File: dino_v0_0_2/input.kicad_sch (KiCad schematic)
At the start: 11 parts, among them SW1 SW_DIP_x08

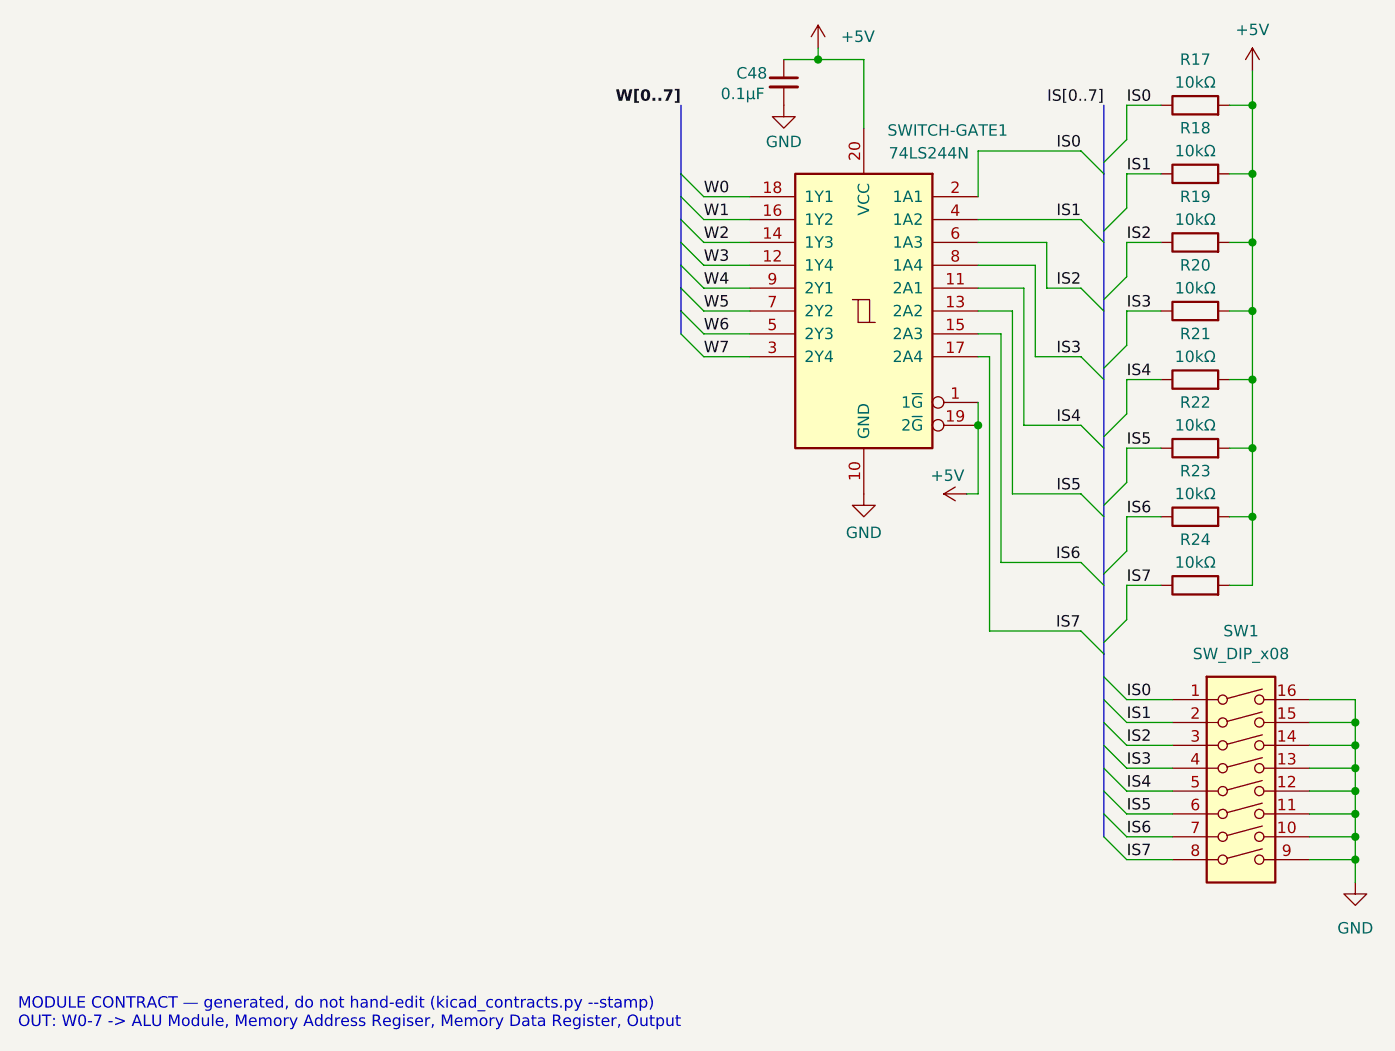
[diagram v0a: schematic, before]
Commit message: feat: card zero's '138 lands in schematic
U76 decodes M11-M13 with E1 on ~{IO_RD_Q}; O0 drives SWITCH_EN
to SWITCH-GATE1's two ~G pins, replacing step A's +5V strap.
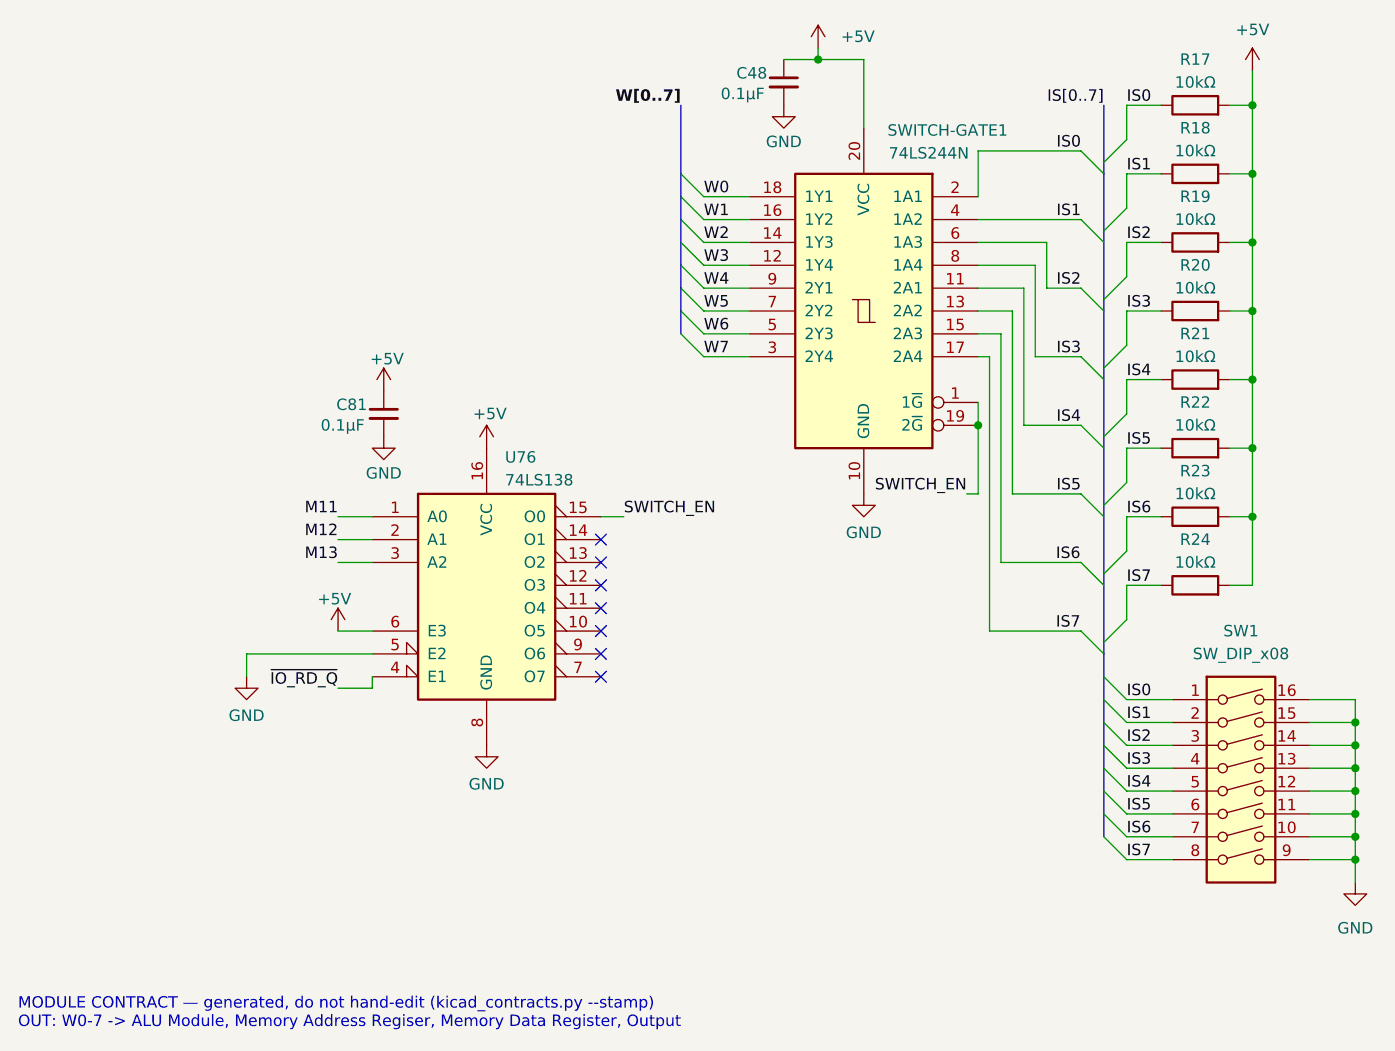
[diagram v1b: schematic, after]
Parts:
- added C81: 0.1µF, symbol Device:C_Small
- added U76: 74LS138, symbol 74xx:74LS138
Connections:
- net +5V: now also C81.1, U76.16 (VCC), U76.6 (E3); no longer SWITCH-GATE1.1 (1~{G}), SWITCH-GATE1.19 (2~{G})
- net GND: now also C81.2, U76.5 (E2), U76.8 (GND)
- new net M11: U76.1 (A0)
- new net M12: U76.2 (A1)
- new net M13: U76.3 (A2)
- new net SWITCH_EN: SWITCH-GATE1.1 (1~{G}), SWITCH-GATE1.19 (2~{G}), U76.15 (O0)
- new net ~{IO_RD_Q}: U76.4 (E1)
- no-connect marks 0 -> 7
